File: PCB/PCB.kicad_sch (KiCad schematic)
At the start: 2 parts, among them J1 Conn_01x08, U1 RASPBERRY_PI_ZERO_2_W

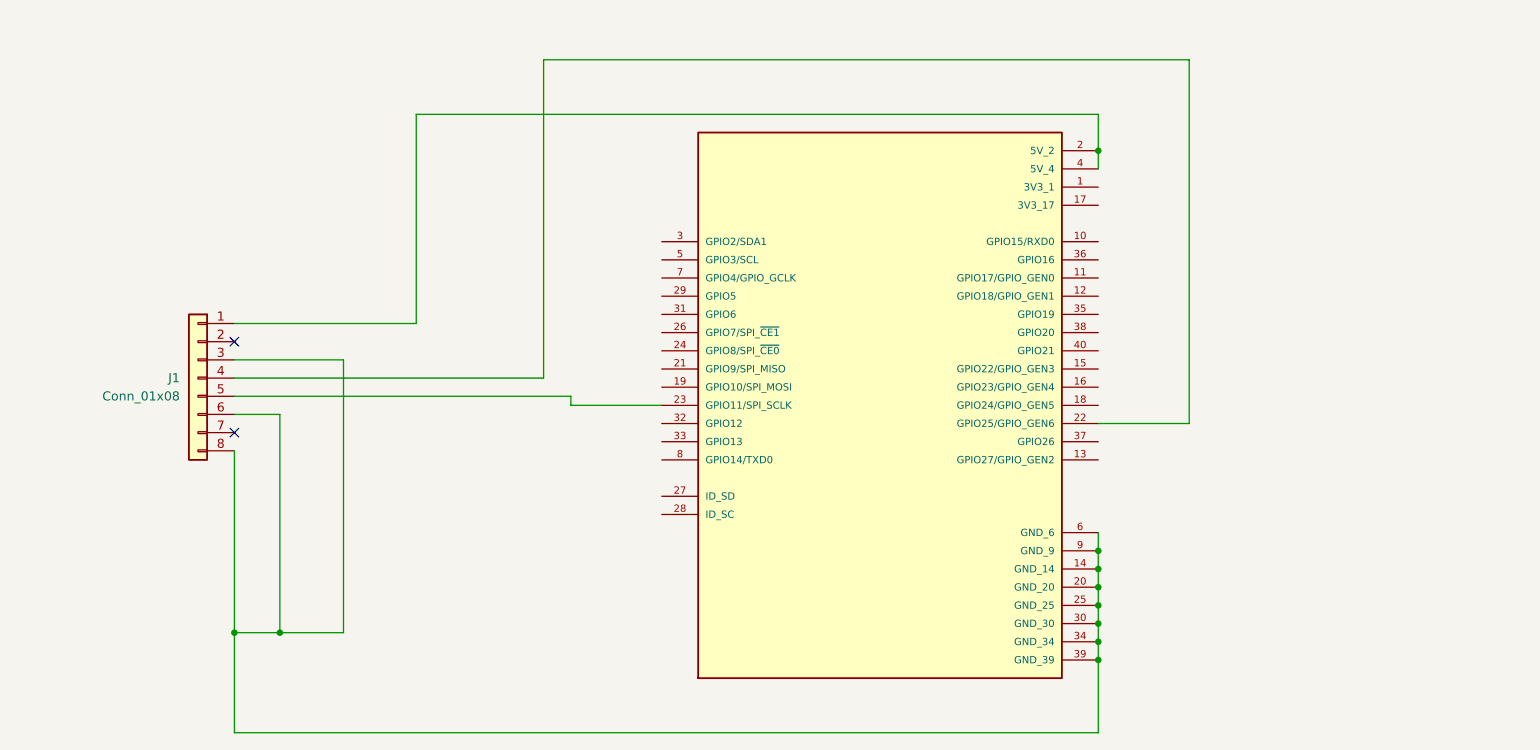
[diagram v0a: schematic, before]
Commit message: finnished PCB and did a notes.md
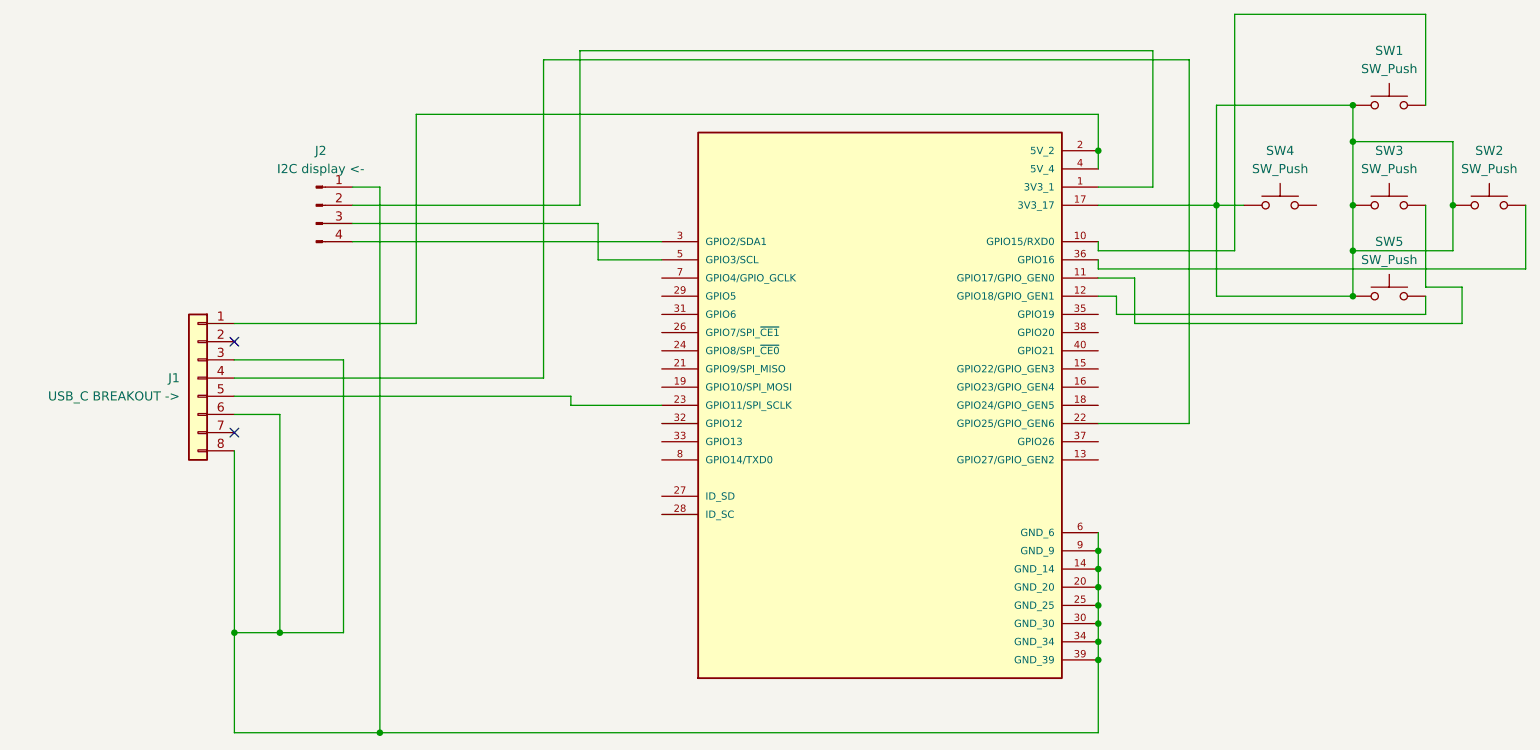
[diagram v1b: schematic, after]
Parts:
- added J2: I2C display <-, Connector_PinHeader_2.54mm:PinHeader_1x04_P2.54mm_Vertical, symbol Connector:Conn_01x04_Pin
- added SW1, SW2, SW3, SW4, SW5: SW_Push, Button_Switch_THT:SW_SPST_Omron_B3F-40xx, symbol Switch:SW_Push
- J1: value Conn_01x08 -> USB_C BREAKOUT ->
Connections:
- net at J1.3 (Pin_3), J1.6 (Pin_6), J1.8 (Pin_8)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: now also J2.1 (Pin_1)
- net at U1.1 (3V3_1): now also J2.2 (Pin_2)
- net at U1.10 (GPIO15/RXD0): now also SW1.2
- net at U1.11 (GPIO17/GPIO_GEN0): now also SW3.2
- net at U1.12 (GPIO18/GPIO_GEN1): now also SW5.2
- net at U1.17 (3V3_17): now also SW1.1, SW2.1, SW3.1, SW4.1, SW5.1
- net at U1.3 (GPIO2/SDA1): now also J2.4 (Pin_4)
- net at U1.36 (GPIO16): now also SW2.2
- net at U1.5 (GPIO3/SCL): now also J2.3 (Pin_3)
